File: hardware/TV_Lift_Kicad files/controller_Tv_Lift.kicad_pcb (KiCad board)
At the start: 4 copper layers, 70 x 157.5 mm, 97 parts, among them J1 socket LAN8720a, J10 CONN_IR_OUT, J11 DRY CONTACT UP DOWN, J12 DRY CONTACT, J2 POWER 24V, J3 CAN_bus, J4 ENCODER, J5 ENCODER_POWER, J6 CONN_RS232, J7 M1 LIMIT UP DOWN, J8 Signal PWR, J9 MOTOR_OUT, Q1 2N3904, SW1 UP, SW2 DOWN, SW3 STOP, SW4 Reset, U1 MAX3232, U10 VNH5019A-E, U2 TSOP32S40F, U3 SN65HVD230, U4 ESP32-WROOM-32, U5 LM2596S-5, U6 AMS1117-3.3, U7 PC817, U8 PC817, U9 NCS1S1205SC

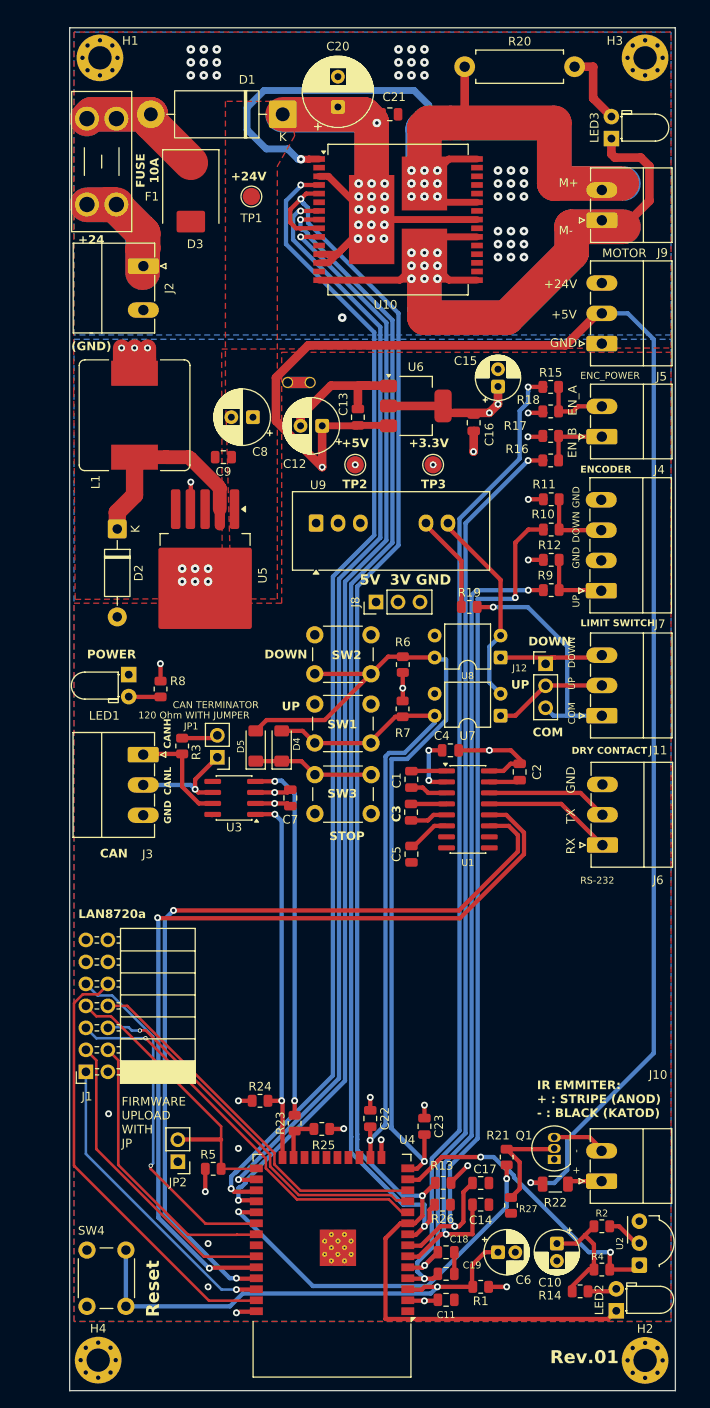
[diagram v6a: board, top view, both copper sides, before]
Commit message: fix bom list of connectors
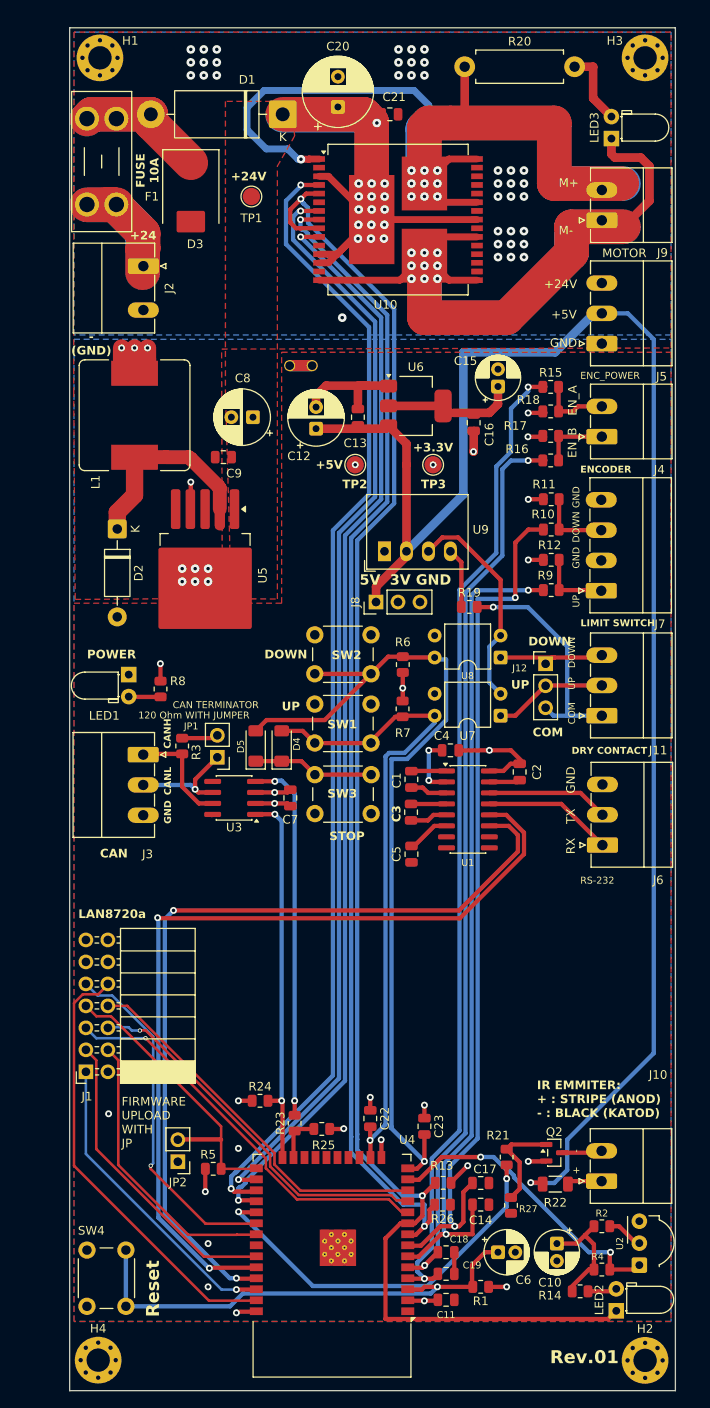
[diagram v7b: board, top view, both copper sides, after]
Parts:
- removed Q1: 2N3904, Package_TO_SOT_THT:TO-92_Inline
- added Q2: MMBT3906, Package_TO_SOT_SMD:SOT-23, F.Cu at (121.5, 155.5)
- C1, C2, C3, C4, C5: value 0.1 uF 16V -> 100 nF 50V
- C11, C13, C14, C17, C22, C23, C7: value 0.1 uF 16V -> 100 nF 16V
- C12: value 150 uF 16V -> 470 uF 16V
- C16: value 0.1 uF 10V -> 100 nF 10V
- C21, C9: value 0.1 uF 50V -> 100 nF 50V
- F1: value Fuse_Mini_10A -> C5249699
- J11: value DRY CONTACT UP DOWN -> 1844223
- J12: value DRY CONTACT -> C5360899
- J2: value POWER 24V -> 1836189
- J3: value CAN_bus -> 1844223
- J4: value ENCODER -> 1844210
- J5: value ENCODER_POWER -> 1844223
- J6: value CONN_RS232 -> 1844223
- J7: value M1 LIMIT UP DOWN -> 1844236
- J8: value Signal PWR -> C5360899
- J9: value MOTOR_OUT -> 1844210
- U9: value NCS1S1205SC -> b0505s-1we; footprint Converter_DCDC:Converter_DCDC_Murata_NCS1SxxxxSC_THT -> Converter_DCDC:Converter_DCDC_RECOM_R-78S-0.1_THT
- moved U9 8.55 mm to (101.9, 86.0)
- moved NT2 1.96 mm to (93.5, 64.5)
- moved C12 0.78 mm to (94.0, 71.8), turned to 90 degrees
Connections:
- U9 pad 3: unconnected-(U9-Control-Pad3) -> Net-(U9--VOUT)
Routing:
- net +5V: track 191.5 -> 200.6 mm, vias 7 -> 6
- net Net-(U9-+VOUT): track 11.4 -> 6.95 mm
- net Net-(J10-Pin_2): track 6.92 -> 4.62 mm
- net Net-(U9--VOUT): track 23.3 -> 25.3 mm
- net /ENC_B: track 104.2 -> 105.4 mm
- net GND: track 37.1 -> 36.6 mm, vias 10 -> 11
- net +3.3V: vias 17 -> 15
